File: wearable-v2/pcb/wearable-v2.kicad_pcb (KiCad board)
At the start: 2 copper layers, 112.1 x 40.2 mm, 109 parts, among them IC1 TESEO-LIV3F, J1 HERALD_V2_CONN_RECEPTACLE, J16 EA_WF030-39S, J17 JST_AUDIO_OUT, J18 DEBUG_HERALD, J19 FTDI_HERALD, J2 HERALD_V2_CONN_RECEPTACLE, J3 HERALD_V2_CONN_RECEPTACLE, J4 HERALD_V2_CONN_RECEPTACLE, J5 HERALD_V2_CONN_PORT, J6 HERALD_V2_CONN_PORT, J7 USB_C_Receptacle_USB2.0, J8 HERALD_V2_CONN_PORT, J9 HERALD_V2_CONN_PORT, SW1 SW_Push, U1 DT1446-04V, U10 ATmega328PB-M, U11 TMP1075, U12 MAX30102, U13 TPA6139A2RGTR, U14 LIS2DE12, U15 TLV751, U16 DRV2605LDGS, U2 MCP73831/2-2MC, U3 TCA6408A, U4 FT201XQ, U5 MX25R8035FZUIL0, U6 BC833, U7 MX25R8035FZxxx0, U8 PCF85063ATL, U9 APDS-9250, Y1 32.768kHz, Y2 8Mhz

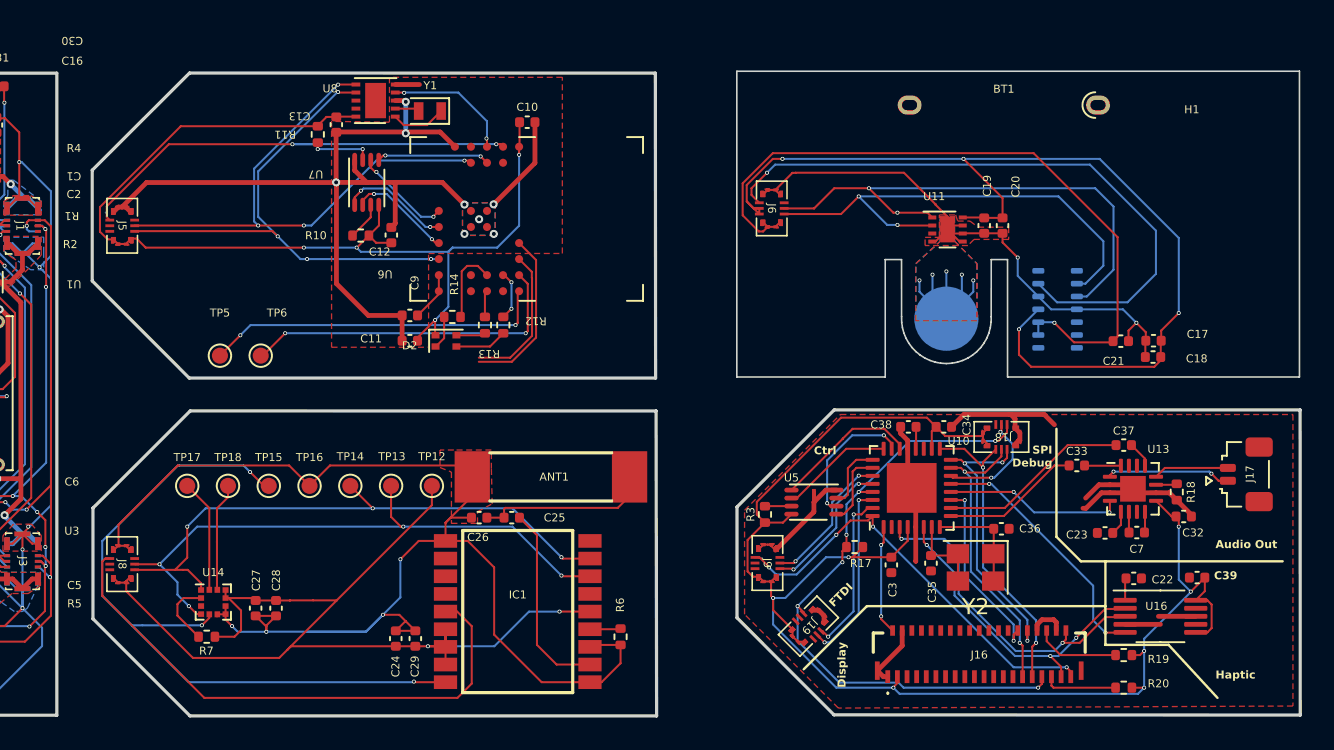
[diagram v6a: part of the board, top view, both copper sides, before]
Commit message: Upgraded flash and corrected XIF placement
Signed-off-by: Adam Fowler <adam@adamfowler.org>
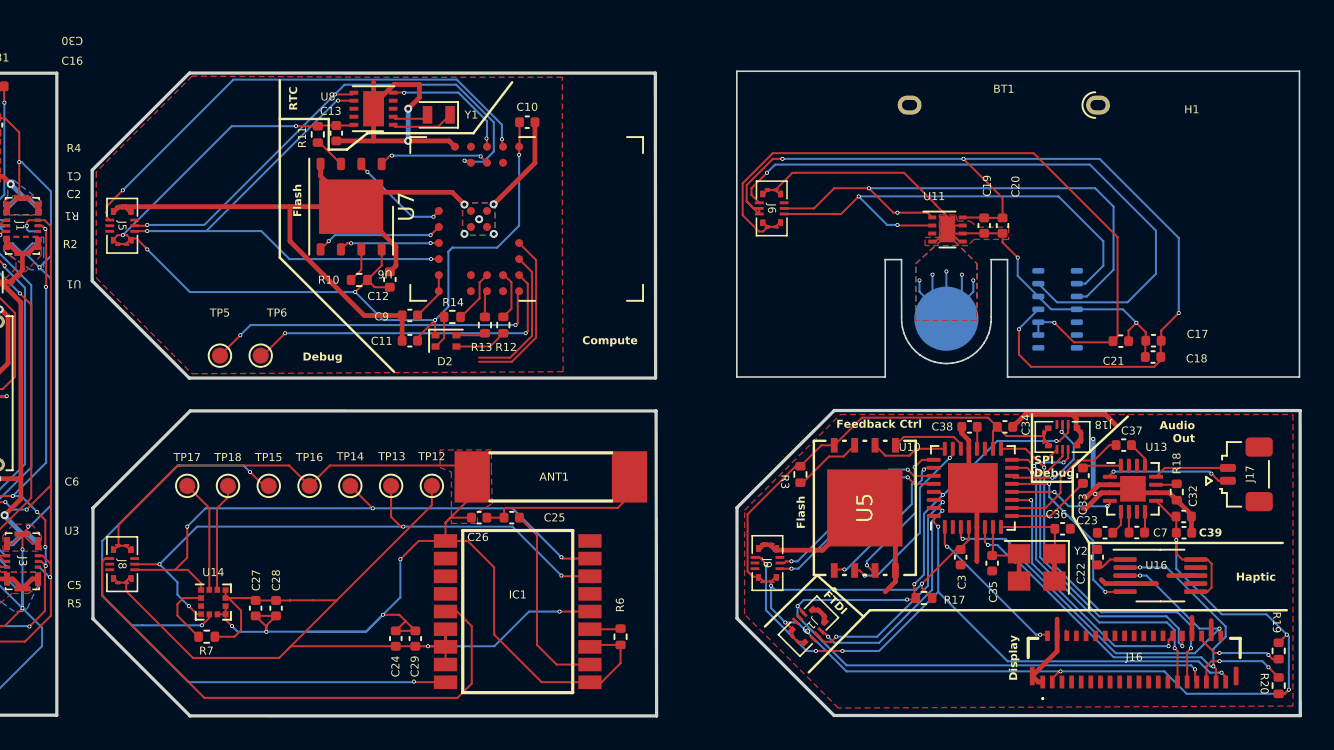
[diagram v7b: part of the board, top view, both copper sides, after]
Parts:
- U5: value MX25R8035FZUIL0 -> MX25R6435FZNIL0; footprint Herald:USON-8-1EP_2x3mm_P0.5mm_EP0.25x1.65mm -> Herald:8-WSON_MAC
- U7: value MX25R8035FZxxx0 -> MX25R6435F; footprint Herald:USON-8-1EP_2x3mm_P0.5mm_EP0.25x1.65mm -> Package_SON:WSON-8-1EP_6x5mm_P1.27mm_EP3.4x4mm
- moved J16 9.66 mm to (167.4, 136.1)
- moved R19 9.66 mm to (176.4, 135.3), turned to -90 degrees
- moved R20 9.65 mm to (176.4, 137.4), turned to 90 degrees
- moved R17 5.36 mm to (154.3, 132.0)
- moved C3 4.34 mm to (156.6, 129.4)
- moved C34 3.81 mm to (159.4, 121.3)
- moved C35 3.81 mm to (158.6, 129.8)
- moved C36 3.81 mm to (162.9, 127.6)
- moved C38 3.81 mm to (157.1, 121.3)
- moved J18 3.81 mm to (162.9, 121.9)
- moved U10 3.81 mm to (157.4, 125.1)
- moved Y2 3.81 mm to (161.3, 130.0)
- moved R3 3.33 mm to (146.6, 124.3), turned to -90 degrees
- moved U5 3.19 mm to (150.6, 126.3), turned to 90 degrees
- moved C39 2.91 mm to (170.5, 127.9), turned to 0 degrees
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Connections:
- J17 pad MP: (no net) -> GND
- U10 pad 25: /Display Board V1/FB_FLASH_WP -> /Display Board V1/FB_FLASH_SEL
- U10 pad 26: /Display Board V1/FB_FLASH_SEL -> /Display Board V1/FB_FLASH_WP
- U8 pad EP: unconnected-(U8-PadEP) -> GND
- Y2 pad 3: (no net) -> Net-(U10-XTAL1/PB6)
- Y2 pad 4: (no net) -> Net-(U10-XTAL2/PB7)
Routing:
- net GND: track 355.7 -> 383.5 mm, vias 44 -> 45
- net /Display Board V1/FB_INT: track 26.4 -> 42.3 mm
- net /Display Board V1/FB_AVR_RESET: track 40.6 -> 53.5 mm
- net VDD: track 358.7 -> 371.4 mm, vias 23 -> 25
- net /Display Board V1/FB_SCL: track 20.1 -> 30.6 mm
- net /Display Board V1/FB_SCA: track 20.9 -> 29.2 mm, vias 2 -> 3
- net /Bio Board V1/SCL: track 151.5 -> 158.3 mm, vias 15 -> 14
- net /Display Board V1/FB_FLASH_SEL: track 4.68 -> 10.3 mm, vias 0 -> 2
- net /Display Board V1/DISP_DCX: track 19.1 -> 24.7 mm
- net /Display Board V1/DISP_SDA: track 18.4 -> 23.4 mm
- net /Display Board V1/DISP_SDO: track 17.6 -> 22.5 mm
- net /Display Board V1/DISP_CSX: track 11.6 -> 16.5 mm
- net /Display Board V1/FB_FLASH_WP: track 4.21 -> 8.99 mm, vias 0 -> 2
- net /Display Board V1/FB_AUDIO_SEL: track 11.1 -> 6.72 mm
- net /Display Board V1/FB_MOSI1: track 9.02 -> 4.77 mm
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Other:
- outline, holes or cut-outs redrawn
- board text added: "Compute"
- board text added: "Debug"
- board text added: "EXT 4 DISPLAY + FEEDBACK BOTTOM NB Components point UP (Toward Connector) Nothing points DOWN (Toward skin) NB Connector points UP (Away from skin, toward Connector board) NB ZIF connector extends out the top of this board and wraps around the top boards, then the battery, to connect to the display"
- board text added: "Feedback Ctrl"
- board text added: "Flash"
- board text added: "RTC"
- board text removed: "Ctrl"
- board text removed: "EXT 4 DISPLAY + FEEDBACK BOTTOM NB Components point UP (Toward Connector) Nothing points DOWN (Toward skin) NB Connector points UP (Away from skin, toward Connector board) NB ZIF connector extends out the bottom of this board and wraps around the top boards, then the battery, to connect to the display"

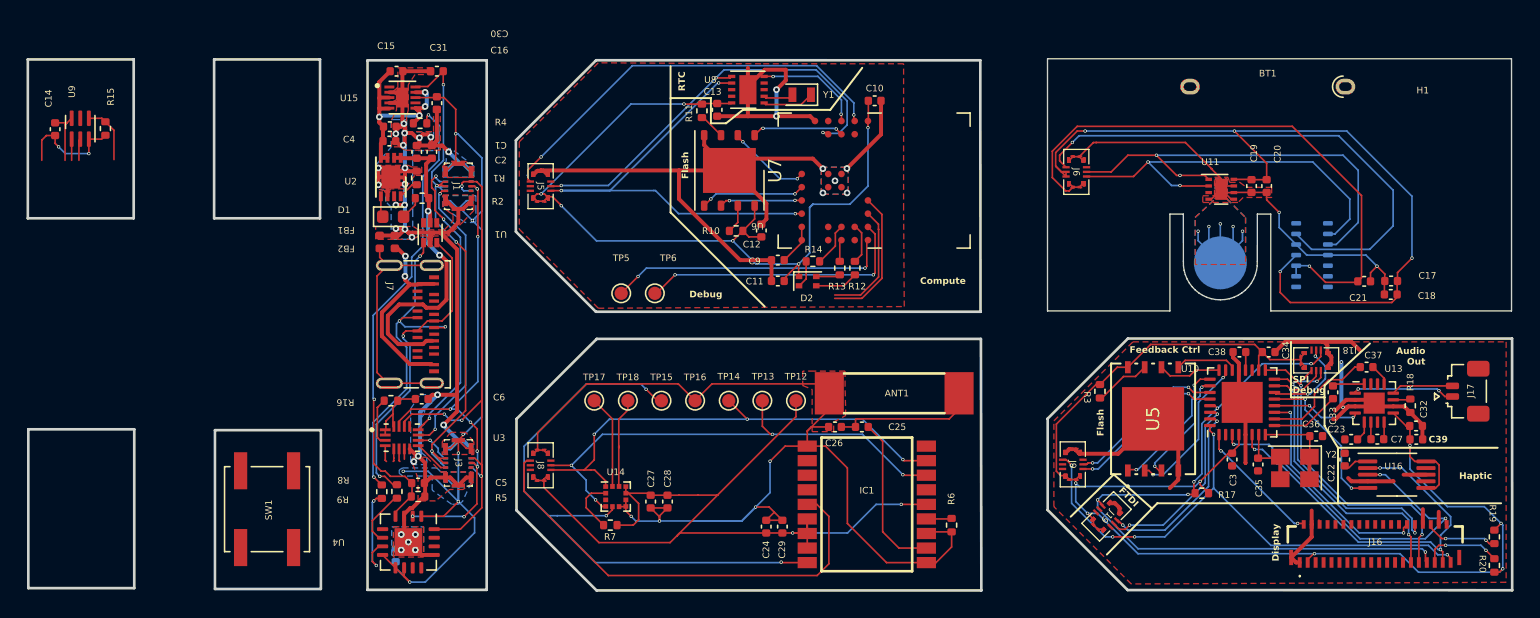
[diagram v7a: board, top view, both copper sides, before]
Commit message: Updated LRA, BOM. Added first 3D model
Signed-off-by: Adam Fowler <adam@adamfowler.org>
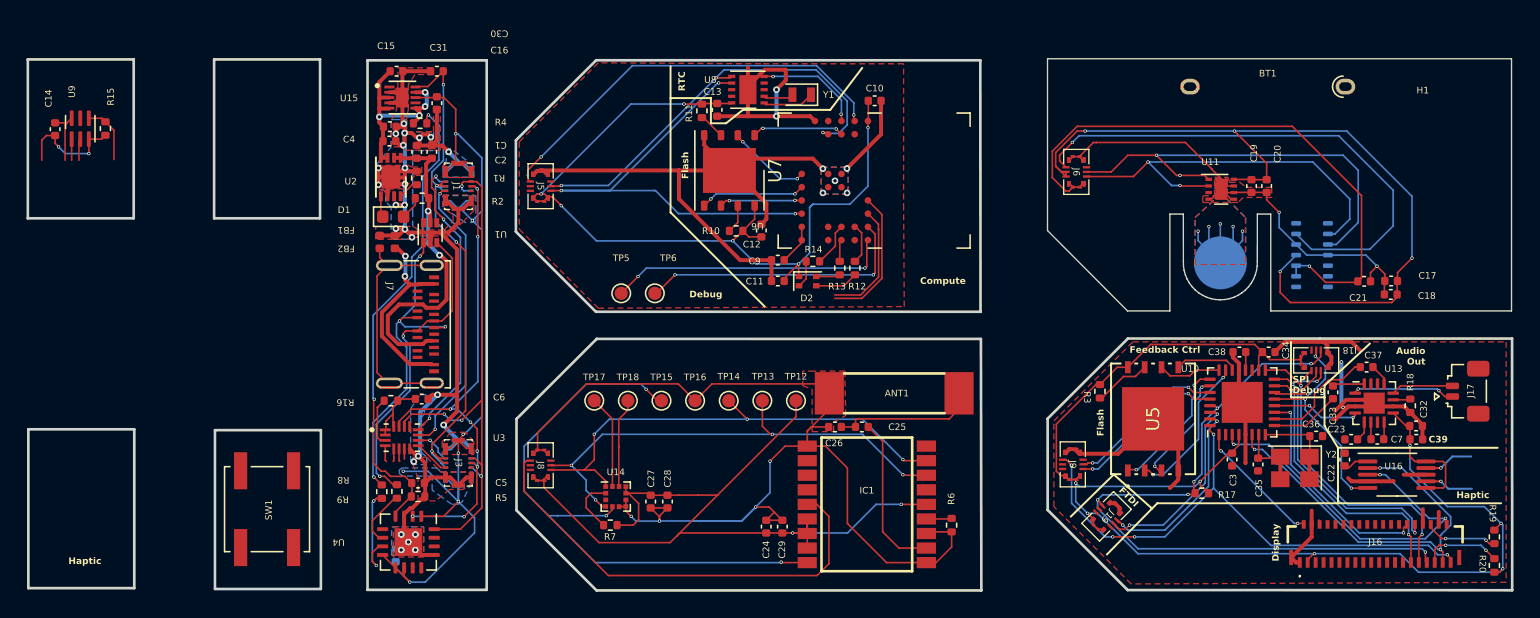
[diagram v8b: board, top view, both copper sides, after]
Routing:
- net /Display Board V1/FB_LRA-: track 0.00 -> 3.77 mm, vias 0 -> 1
- net /Display Board V1/FB_LRA+: track 0.00 -> 3.70 mm, vias 0 -> 1
- net VDD: track 371.4 -> 372.5 mm
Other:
- outline, holes or cut-outs redrawn
- board text added: "FRONT 2 TOP BUTTON TOP RIGHT"
- board text added: "FRONT 3 HAPTIC MOTOR BUTTOM LEFT"
- board text added: "FRONT 4 BOTTOM BUTTON BUTTOM RIGHT"
- board text removed: "FRONT 2 GNSS ANTENNA TOP RIGHT"
- board text removed: "FRONT 3 LEFT BUTTON BUTTOM LEFT"
- board text removed: "FRONT 4 RIGHT BUTTON BUTTOM RIGHT"
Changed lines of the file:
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@@
       (xy 177.750011 139.2854)
       (xy 177.739766 120.276)
+      (xy 163.229266 120.2745)
       (xy 148.718766 120.273)
     )
@@
   (gr_poly
     (pts
-      (xy 142.647 118.187)
+      (xy 142.647 112.1156)
+      (xy 148.6916 118.187)
       (xy 151.892 118.187)
       (xy 151.892 110.871)
@@
     (effects (font (size 0.5 0.5) (thickness 0.125) bold) (justify bottom))
   )
-  (gr_text "Haptic" (at 173.736 130.937) (layer "F.SilkS")
+  (gr_text "Haptic" (at 173.5328 132.3848) (layer "F.SilkS")
     (effects (font (size 0.5 0.5) (thickness 0.125) bold) (justify left bottom))
   )
@@
     (effects (font (size 0.5 0.5) (thickness 0.125) bold) (justify bottom))
   )
+  (gr_text "Haptic" (at 68.6816 137.3632) (layer "F.SilkS")
+    (effects (font (size 0.5 0.5) (thickness 0.125) bold) (justify left bottom))
+  )
   (gr_text "FTDI" (at 147.955 131.826 -45) (layer "F.SilkS")
     (effects (font (size 0.5 0.5) (thickness 0.125) bold) (justify left bottom))
@@
     (effects (font (size 1 1) (thickness 0.2) bold) (justify left bottom))
   )
-  (gr_text "FRONT 3 LEFT BUTTON\nBUTTOM LEFT" (at 31.877 135.001) (layer "Cmts.User")
+  (gr_text "FRONT 3 HAPTIC MOTOR\nBUTTOM LEFT" (at 31.877 135.001) (layer "Cmts.User")
     (effects (font (size 1.5 1.5) (thickness 0.3) bold) (justify left bottom))
   )
@@
     (effects (font (size 1 1) (thickness 0.25) bold) (justify bottom))
   )
-  (gr_text "FRONT 4 RIGHT BUTTON\nBUTTOM RIGHT" (at 88.011 146.685) (layer "Cmts.User")
+  (gr_text "FRONT 4 BOTTOM BUTTON\nBUTTOM RIGHT" (at 88.011 146.685) (layer "Cmts.User")
     (effects (font (size 1.5 1.5) (thickness 0.3) bold) (justify right bottom))
   )
-  (gr_text "FRONT 2 GNSS ANTENNA\nTOP RIGHT" (at 87.503 92.837) (layer "Cmts.User")
+  (gr_text "FRONT 2 TOP BUTTON\nTOP RIGHT" (at 87.503 92.837) (layer "Cmts.User")
     (effects (font (size 1.5 1.5) (thickness 0.3) bold) (justify right bottom))
   )
@@
     (effects (font (size 1.5 1.5) (thickness 0.3) bold) (justify left bottom))
   )
-  (gr_text_box "LRA here"
-    (start 172.575 128.896) (end 176.892 132.715) (layer "Cmts.User")
-      (effects (font (size 1 1) (thickness 0.25) bold) (justify left top))
-    (stroke (width 0.2) (type solid))  )
   (dimension (type aligned) (layer "F.SilkS")
     (pts (xy 177.8 138.684) (xy 175.006 138.684))
@@
   (segment (start 110.9828 131.957) (end 111.76 132.7342) (width 0.127) (layer "F.Cu") (net 5))
   (segment (start 105.8194 110.1374) (end 105.8194 110.125) (width 0.127) (layer "F.Cu") (net 5))
-  (segment (start 172.2255 129.8195) (end 172.2255 131.3045) (width 0.127) (layer "F.Cu") (net 5))
-  (segment (start 171.962 129.556) (end 172.2255 129.8195) (width 0.127) (layer "F.Cu") (net 5))
   (segment (start 92.668 127.113) (end 92.668 126.508) (width 0.127) (layer "F.Cu") (net 5))
   (segment (start 67.681 104.937) (end 67.021 104.937) (width 0.127) (layer "F.Cu") (net 5))
@@
   (segment (start 162.74822 136.525) (end 162.3016 136.97162) (width 0.127) (layer "F.Cu") (net 5))
   (segment (start 144.572 108.8324) (end 144.286 109.1184) (width 0.127) (layer "F.Cu") (net 5))
+  (segment (start 172.72 131.3688) (end 172.5328 131.556) (width 0.127) (layer "F.Cu") (net 5))
   (segment (start 144.78 131.191) (end 144.78 130.9256) (width 0.127) (layer "F.Cu") (net 5))
   (segment (start 154.178 131.064) (end 154.178 131.316) (width 0.127) (layer "F.Cu") (net 5))
@@
   (segment (start 124.459 134.96) (end 121.4 134.96) (width 0.127) (layer "F.Cu") (net 5))
   (segment (start 124.498 134.999) (end 124.459 134.96) (width 0.127) (layer "F.Cu") (net 5))
+  (segment (start 171.237 129.556) (end 172.5328 129.556) (width 0.127) (layer "F.Cu") (net 5))
   (segment (start 104.8562 109.6237) (end 104.5812 109.8987) (width 0.127) (layer "F.Cu") (net 5))
   (segment (start 118.746 102.517) (end 118.79 102.473) (width 0.127) (layer "F.Cu") (net 5))
@@
   (segment (start 144.286 109.1184) (end 144.018 109.1184) (width 0.127) (layer "F.Cu") (net 5))
   (segment (start 131.6 132.8) (end 131.601 132.799) (width 0.127) (layer "F.Cu") (net 5))
+  (segment (start 172.72 129.7432) (end 172.72 131.3688) (width 0.127) (layer "F.Cu") (net 5))
   (segment (start 161.866 122.145) (end 162.141 122.42) (width 0.127) (layer "F.Cu") (net 5))
   (segment (start 156.309 128.933) (end 156.591 128.933) (width 0.127) (layer "F.Cu") (net 5))
@@
   (segment (start 112.519 131.957) (end 110.7953 131.957) (width 0.127) (layer "F.Cu") (net 5))
   (segment (start 145.677838 133.477) (end 145.669 133.477) (width 0.127) (layer "F.Cu") (net 5))
-  (segment (start 171.974 131.556) (end 171.237 131.556) (width 0.127) (layer "F.Cu") (net 5))
   (segment (start 67.681 104.937) (end 67.681 105.527) (width 0.127) (layer "F.Cu") (net 5))
   (segment (start 117.720556 132.104444) (end 117.720556 132.1) (width 0.127) (layer "F.Cu") (net 5))
@@
   (segment (start 143.3165 130.29368) (end 143.64842 130.6256) (width 0.127) (layer "F.Cu") (net 5))
   (segment (start 166.368 115.671) (end 166.088 115.951) (width 0.127) (layer "F.Cu") (net 5))
-  (segment (start 171.237 129.556) (end 171.962 129.556) (width 0.127) (layer "F.Cu") (net 5))
   (segment (start 70.231 105.207) (end 71.191 105.207) (width 0.127) (layer "F.Cu") (net 5))
   (segment (start 144.005 130.6256) (end 144.305 130.9256) (width 0.127) (layer "F.Cu") (net 5))
@@
   (segment (start 98.5012 127.5968) (end 98.141 127.957) (width 0.127) (layer "F.Cu") (net 5))
   (segment (start 113.94 132.108) (end 114.808 132.108) (width 0.127) (layer "F.Cu") (net 5))
+  (segment (start 172.5328 131.556) (end 171.237 131.556) (width 0.127) (layer "F.Cu") (net 5))
   (segment (start 163.6522 116.0272) (end 162.433 114.808) (width 0.127) (layer "F.Cu") (net 5))
   (segment (start 104.6412 109.347) (end 104.8562 109.562) (width 0.127) (layer "F.Cu") (net 5))
@@
   (segment (start 95.37625 133.695) (end 95.34325 133.695) (width 0.127) (layer "F.Cu") (net 5))
   (segment (start 122.7556 115.7328) (end 122.7556 115.9256) (width 0.127) (layer "F.Cu") (net 5))
+  (segment (start 172.5328 129.556) (end 172.72 129.7432) (width 0.127) (layer "F.Cu") (net 5))
   (segment (start 124.498 133.899) (end 124.498 134.999) (width 0.127) (layer "F.Cu") (net 5))
   (segment (start 121.031 112.593) (end 120.086 112.593) (width 0.127) (layer "F.Cu") (net 5))
@@
   (segment (start 123.4 134.96) (end 124.498 134.96) (width 0.127) (layer "F.Cu") (net 5))
   (segment (start 176.782 137.922) (end 176.403 137.922) (width 0.127) (layer "F.Cu") (net 5))
-  (segment (start 172.2255 131.3045) (end 171.974 131.556) (width 0.127) (layer "F.Cu") (net 5))
   (segment (start 143.3165 126.7363) (end 143.3165 130.29368) (width 0.127) (layer "F.Cu") (net 5))
   (segment (start 116.541 102.5632) (end 116.5872 102.517) (width 0.127) (layer "F.Cu") (net 5))
@@
   (segment (start 164.848 130.812) (end 164.848 128.399) (width 0.127) (layer "B.Cu") (net 144))
   (segment (start 165.608 131.572) (end 164.848 130.812) (width 0.127) (layer "B.Cu") (net 144))
+  (segment (start 171.237 131.056) (end 172.3564 131.056) (width 0.15) (layer "F.Cu") (net 148))
+  (segment (start 172.3564 131.056) (end 172.3644 131.064) (width 0.15) (layer "F.Cu") (net 148))
+  (via (at 172.3644 131.064) (size 0.25) (drill 0.15) (layers "F.Cu" "B.Cu") (free) (net 148))
+  (segment (start 172.3644 131.064) (end 172.9232 131.6228) (width 0.15) (layer "B.Cu") (net 148))
+  (segment (start 172.9232 131.6228) (end 174.7012 131.6228) (width 0.15) (layer "B.Cu") (net 148))
+  (segment (start 171.237 130.056) (end 172.3564 130.056) (width 0.15) (layer "F.Cu") (net 149))
+  (segment (start 172.3564 130.056) (end 172.3644 130.048) (width 0.15) (layer "F.Cu") (net 149))
+  (via (at 172.3644 130.048) (size 0.25) (drill 0.15) (layers "F.Cu" "B.Cu") (free) (net 149))
+  (segment (start 172.3644 130.048) (end 173.228 129.1844) (width 0.15) (layer "B.Cu") (net 149))
+  (segment (start 173.228 129.1844) (end 174.6504 129.1844) (width 0.15) (layer "B.Cu") (net 149))
   (segment (start 96.006575 127.959775) (end 96.00435 127.962) (width 0.127) (layer "F.Cu") (net 151))
   (segment (start 96.00435 127.962) (end 95.109 127.962) (width 0.127) (layer "F.Cu") (net 151))
